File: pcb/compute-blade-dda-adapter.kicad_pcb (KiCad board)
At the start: 2 copper layers, 28 x 16.8 mm, 2 parts, among them J1 COMPUTE BLADE, J2 DDA GPS/RTC RIGHT-ANGLE

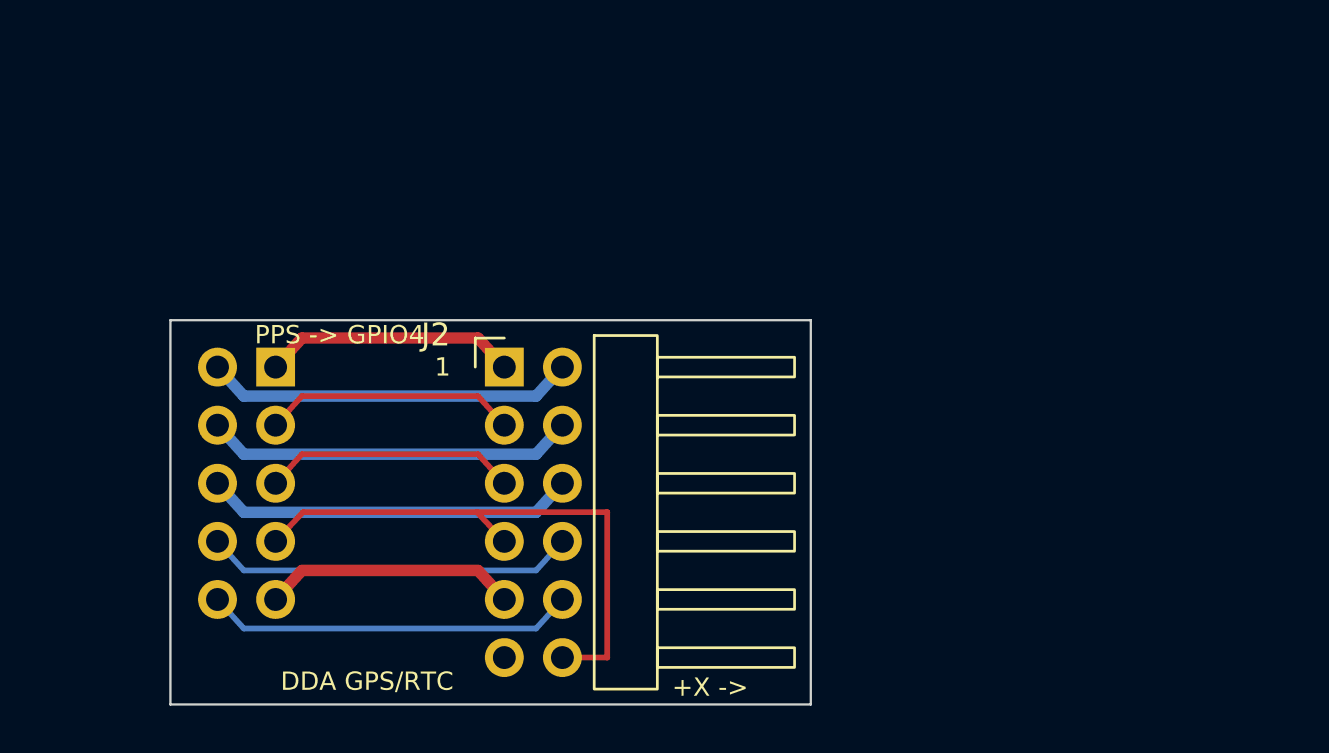
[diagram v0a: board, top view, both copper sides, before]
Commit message: Correct DDA rotation toward SSD side
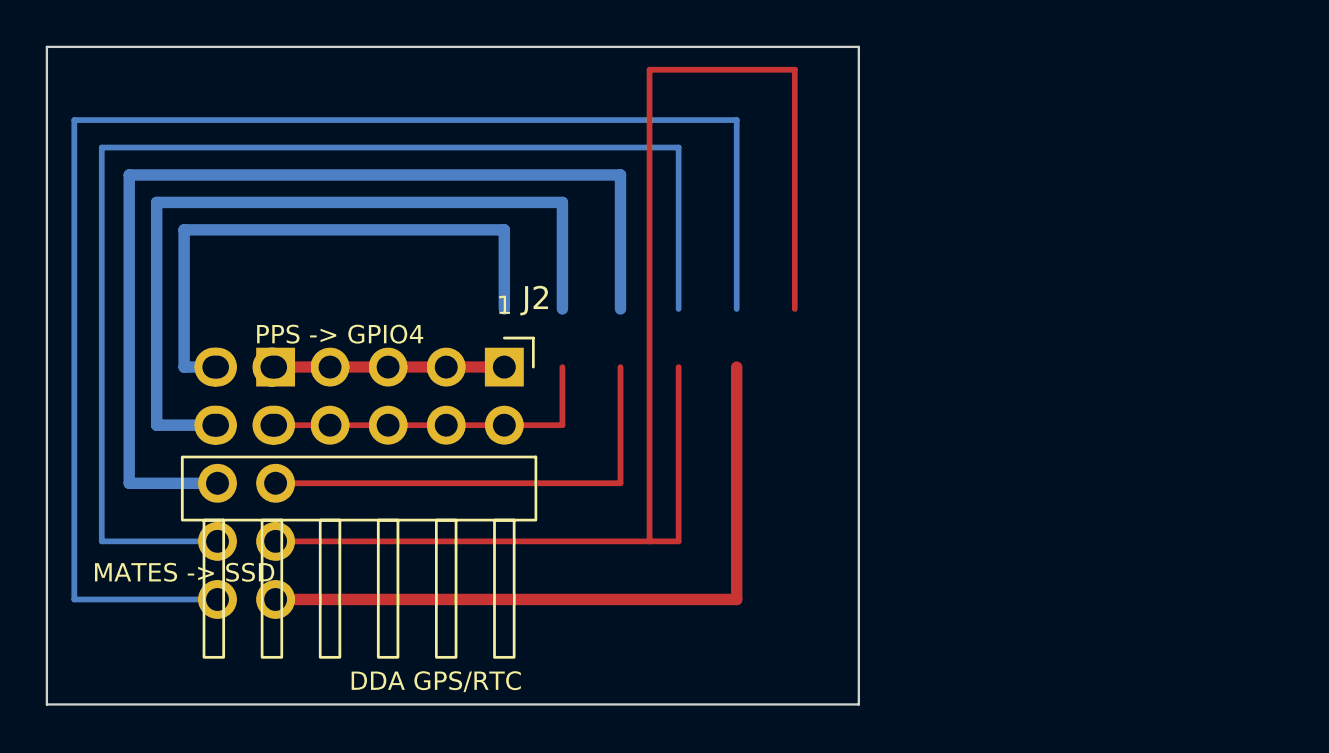
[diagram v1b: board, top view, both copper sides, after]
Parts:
- turned J2 to -90 degrees
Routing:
- net UART_RX_FROM_GPS_TX: track 16.2 -> 64.4 mm
- net UART_TX_TO_GPS_RX: track 16.2 -> 54.6 mm
- net PPS_GPIO4: track 25.1 -> 62.7 mm
- net GND_PIN6: track 16.2 -> 44.7 mm
- net GND_PIN9: track 11.1 -> 30.3 mm
- net 5V_PIN4: track 16.2 -> 34.8 mm
- net SCL_GPIO3: track 11.1 -> 20.2 mm
- net 5V_PIN2: track 16.2 -> 24.9 mm
- net SDA_GPIO2: track 11.1 -> 15.1 mm
- net 3V3: track 11.1 -> 10.0 mm
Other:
- board size 28 x 16.8 mm -> 35.5 x 28.8 mm
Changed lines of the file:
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@@
   (footprint "Connector_PinHeader_2.54mm:PinHeader_2x06_P2.54mm_Horizontal"
     (layer "F.Cu")
-    (at 110 60.16 0)
+    (at 110 60.16 -90)
     (descr "KiCad 10 standard 2x06 2.54 mm horizontal through-hole pin header, 6 mm mating pins")
     (tags "Through hole angled pin header THT 2x06 2.54mm double row")
@@
     (fp_text user "1" (at -2.7 0 0) (layer "F.SilkS")
  (effects (font (size 0.8 0.8) (thickness 0.14))))
-    (fp_text user "+X ->" (at 9 14 0) (layer "F.SilkS")
+    (fp_text user "MATES -> SSD" (at 9 14 0) (layer "F.SilkS")
  (effects (font (size 0.8 0.8) (thickness 0.13))))
     (pad "1" thru_hole rect (at 0 0)
@@
     (model "${KICAD10_3DMODEL_DIR}/Connector_PinHeader_2.54mm.3dshapes/PinHeader_2x06_P2.54mm_Horizontal.step" (offset (xyz 0 0 0)) (scale (xyz 1 1 1)) (rotate (xyz 0 0 0)))
   )
-  (gr_rect (start 95.4 58.11) (end 123.4 74.91)
+  (gr_rect (start 90 46.16) (end 125.5 74.91)
     (stroke (width 0.1) (type default)) (fill none) (layer "Edge.Cuts"))
-  (gr_text "DDA GPS/RTC" (at 104 73.9 0) (layer "F.SilkS")
+  (gr_text "DDA GPS/RTC" (at 107 73.9 0) (layer "F.SilkS")
     (effects (font (size 0.8 0.8) (thickness 0.13))))
   (gr_text "PPS -> GPIO4" (at 102.8 58.75 0) (layer "F.SilkS")
@@
   (gr_text "COMPUTE BLADE" (at 102.2 73.9 0) (layer "B.SilkS")
     (effects (font (size 0.8 0.8) (thickness 0.13)) (justify mirror)))
-  (segment (start 100 60.16) (end 101.15 58.89) (width 0.5) (layer "F.Cu") (net 1))
-  (segment (start 101.15 58.89) (end 108.85 58.89) (width 0.5) (layer "F.Cu") (net 1))
-  (segment (start 108.85 58.89) (end 110 60.16) (width 0.5) (layer "F.Cu") (net 1))
-  (segment (start 97.46 60.16) (end 98.61 61.43) (width 0.5) (layer "B.Cu") (net 2))
-  (segment (start 98.61 61.43) (end 111.39 61.43) (width 0.5) (layer "B.Cu") (net 2))
-  (segment (start 111.39 61.43) (end 112.54 60.16) (width 0.5) (layer "B.Cu") (net 2))
-  (segment (start 100 62.7) (end 101.15 61.43) (width 0.25) (layer "F.Cu") (net 3))
-  (segment (start 101.15 61.43) (end 108.85 61.43) (width 0.25) (layer "F.Cu") (net 3))
-  (segment (start 108.85 61.43) (end 110 62.7) (width 0.25) (layer "F.Cu") (net 3))
-  (segment (start 97.46 62.7) (end 98.61 63.97) (width 0.5) (layer "B.Cu") (net 4))
-  (segment (start 98.61 63.97) (end 111.39 63.97) (width 0.5) (layer "B.Cu") (net 4))
-  (segment (start 111.39 63.97) (end 112.54 62.7) (width 0.5) (layer "B.Cu") (net 4))
-  (segment (start 100 65.24) (end 101.15 63.97) (width 0.25) (layer "F.Cu") (net 5))
-  (segment (start 101.15 63.97) (end 108.85 63.97) (width 0.25) (layer "F.Cu") (net 5))
-  (segment (start 108.85 63.97) (end 110 65.24) (width 0.25) (layer "F.Cu") (net 5))
-  (segment (start 97.46 65.24) (end 98.61 66.51) (width 0.5) (layer "B.Cu") (net 6))
-  (segment (start 98.61 66.51) (end 111.39 66.51) (width 0.5) (layer "B.Cu") (net 6))
-  (segment (start 111.39 66.51) (end 112.54 65.24) (width 0.5) (layer "B.Cu") (net 6))
-  (segment (start 100 67.78) (end 101.2 66.5) (width 0.25) (layer "F.Cu") (net 7))
-  (segment (start 101.2 66.5) (end 108.8 66.5) (width 0.25) (layer "F.Cu") (net 7))
-  (segment (start 108.8 66.5) (end 110 67.78) (width 0.25) (layer "F.Cu") (net 7))
-  (segment (start 97.46 67.78) (end 98.61 69.05) (width 0.25) (layer "B.Cu") (net 8))
-  (segment (start 98.61 69.05) (end 111.39 69.05) (width 0.25) (layer "B.Cu") (net 8))
-  (segment (start 111.39 69.05) (end 112.54 67.78) (width 0.25) (layer "B.Cu") (net 8))
-  (segment (start 100 70.32) (end 101.15 69.05) (width 0.5) (layer "F.Cu") (net 9))
-  (segment (start 101.15 69.05) (end 108.85 69.05) (width 0.5) (layer "F.Cu") (net 9))
-  (segment (start 108.85 69.05) (end 110 70.32) (width 0.5) (layer "F.Cu") (net 9))
-  (segment (start 97.46 70.32) (end 98.61 71.59) (width 0.25) (layer "B.Cu") (net 10))
-  (segment (start 98.61 71.59) (end 111.39 71.59) (width 0.25) (layer "B.Cu") (net 10))
-  (segment (start 111.39 71.59) (end 112.54 70.32) (width 0.25) (layer "B.Cu") (net 10))
-  (segment (start 112.54 72.86) (end 114.5 72.86) (width 0.25) (layer "F.Cu") (net 7))
-  (segment (start 114.5 72.86) (end 114.5 66.5) (width 0.25) (layer "F.Cu") (net 7))
-  (segment (start 114.5 66.5) (end 108.8 66.5) (width 0.25) (layer "F.Cu") (net 7))
+  (segment (start 100 60.16) (end 110 60.16) (width 0.5) (layer "F.Cu") (net 1))
+  (segment (start 97.46 60.16) (end 96 60.16) (width 0.5) (layer "B.Cu") (net 2))
+  (segment (start 96 60.16) (end 96 54.16) (width 0.5) (layer "B.Cu") (net 2))
+  (segment (start 96 54.16) (end 110 54.16) (width 0.5) (layer "B.Cu") (net 2))
+  (segment (start 110 54.16) (end 110 57.62) (width 0.5) (layer "B.Cu") (net 2))
+  (segment (start 100 62.7) (end 112.54 62.7) (width 0.25) (layer "F.Cu") (net 3))
+  (segment (start 112.54 62.7) (end 112.54 60.16) (width 0.25) (layer "F.Cu") (net 3))
+  (segment (start 97.46 62.7) (end 94.8 62.7) (width 0.5) (layer "B.Cu") (net 4))
+  (segment (start 94.8 62.7) (end 94.8 52.96) (width 0.5) (layer "B.Cu") (net 4))
+  (segment (start 94.8 52.96) (end 112.54 52.96) (width 0.5) (layer "B.Cu") (net 4))
+  (segment (start 112.54 52.96) (end 112.54 57.62) (width 0.5) (layer "B.Cu") (net 4))
+  (segment (start 100 65.24) (end 115.08 65.24) (width 0.25) (layer "F.Cu") (net 5))
+  (segment (start 115.08 65.24) (end 115.08 60.16) (width 0.25) (layer "F.Cu") (net 5))
+  (segment (start 97.46 65.24) (end 93.6 65.24) (width 0.5) (layer "B.Cu") (net 6))
+  (segment (start 93.6 65.24) (end 93.6 51.76) (width 0.5) (layer "B.Cu") (net 6))
+  (segment (start 93.6 51.76) (end 115.08 51.76) (width 0.5) (layer "B.Cu") (net 6))
+  (segment (start 115.08 51.76) (end 115.08 57.62) (width 0.5) (layer "B.Cu") (net 6))
+  (segment (start 100 67.78) (end 116.35 67.78) (width 0.25) (layer "F.Cu") (net 7))
+  (segment (start 116.35 67.78) (end 117.62 67.78) (width 0.25) (layer "F.Cu") (net 7))
+  (segment (start 117.62 67.78) (end 117.62 60.16) (width 0.25) (layer "F.Cu") (net 7))
+  (segment (start 97.46 67.78) (end 92.4 67.78) (width 0.25) (layer "B.Cu") (net 8))
+  (segment (start 92.4 67.78) (end 92.4 50.56) (width 0.25) (layer "B.Cu") (net 8))
+  (segment (start 92.4 50.56) (end 117.62 50.56) (width 0.25) (layer "B.Cu") (net 8))
+  (segment (start 117.62 50.56) (end 117.62 57.62) (width 0.25) (layer "B.Cu") (net 8))
+  (segment (start 100 70.32) (end 120.16 70.32) (width 0.5) (layer "F.Cu") (net 9))
+  (segment (start 120.16 70.32) (end 120.16 60.16) (width 0.5) (layer "F.Cu") (net 9))
+  (segment (start 97.46 70.32) (end 91.2 70.32) (width 0.25) (layer "B.Cu") (net 10))
+  (segment (start 91.2 70.32) (end 91.2 49.36) (width 0.25) (layer "B.Cu") (net 10))
+  (segment (start 91.2 49.36) (end 120.16 49.36) (width 0.25) (layer "B.Cu") (net 10))
+  (segment (start 120.16 49.36) (end 120.16 57.62) (width 0.25) (layer "B.Cu") (net 10))
+  (segment (start 122.7 57.62) (end 122.7 47.16) (width 0.25) (layer "F.Cu") (net 7))
+  (segment (start 122.7 47.16) (end 116.35 47.16) (width 0.25) (layer "F.Cu") (net 7))
+  (segment (start 116.35 47.16) (end 116.35 67.78) (width 0.25) (layer "F.Cu") (net 7))
 )

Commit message: Use KiCad-correct J2 rotation convention
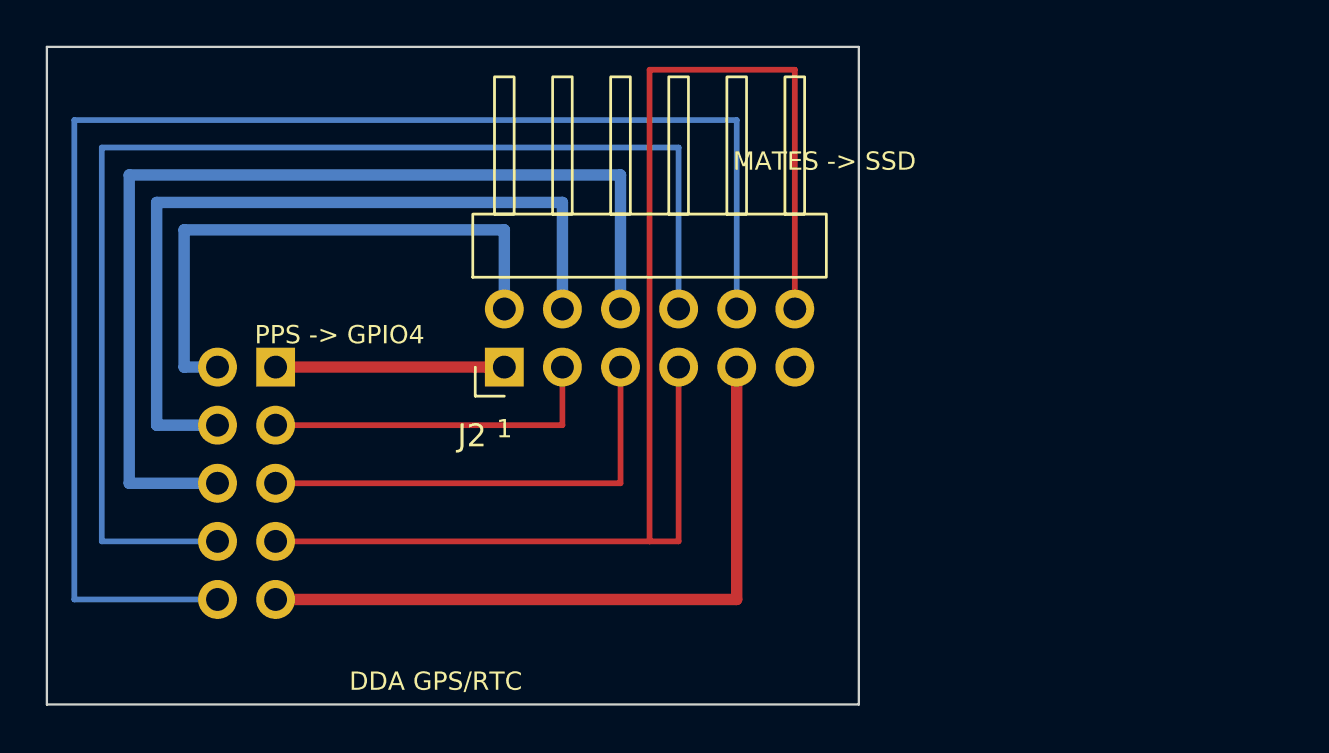
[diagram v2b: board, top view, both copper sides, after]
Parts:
- turned J2 to 90 degrees
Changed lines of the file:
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@@
   (footprint "Connector_PinHeader_2.54mm:PinHeader_2x06_P2.54mm_Horizontal"
     (layer "F.Cu")
-    (at 110 60.16 -90)
+    (at 110 60.16 90)
     (descr "KiCad 10 standard 2x06 2.54 mm horizontal through-hole pin header, 6 mm mating pins")
     (tags "Through hole angled pin header THT 2x06 2.54mm double row")

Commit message: Move upright DDA assembly to positive Y
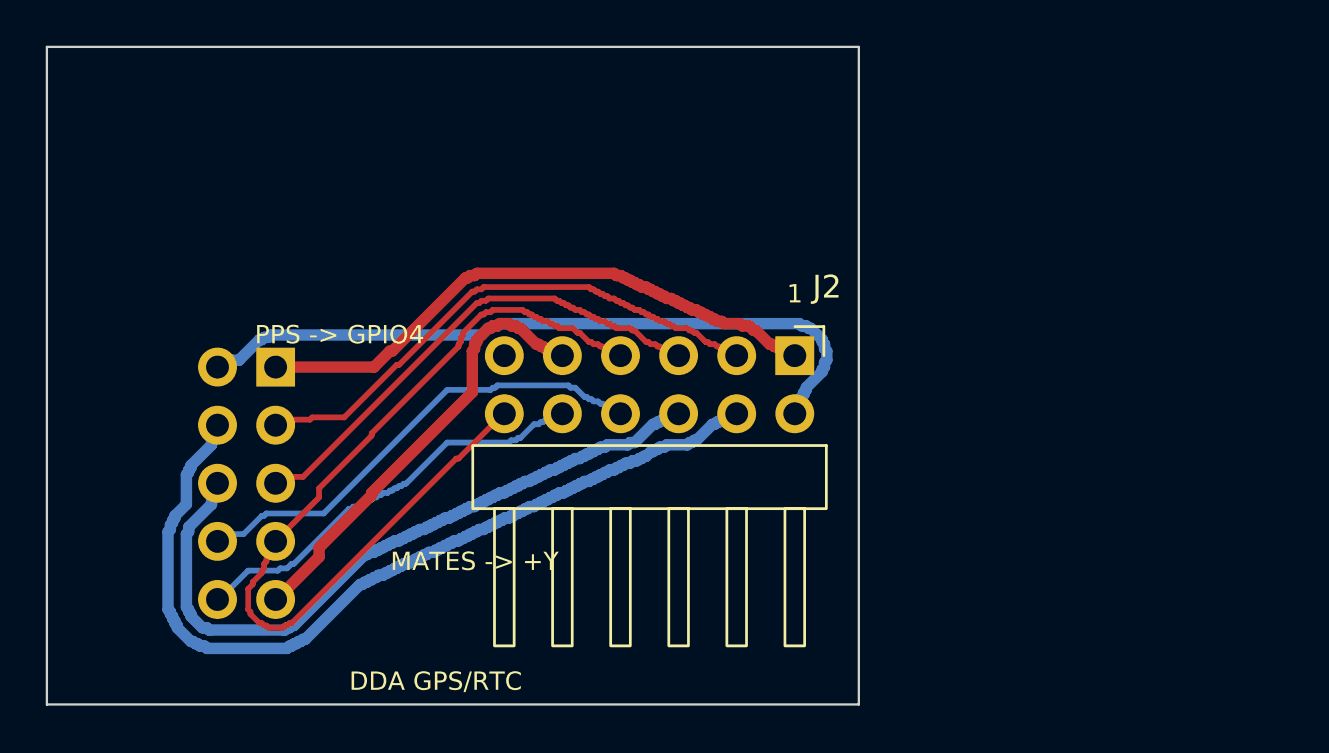
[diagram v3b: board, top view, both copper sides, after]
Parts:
- moved J2 12.7 mm to (122.7, 59.7), turned to -90 degrees
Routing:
- net UART_RX_FROM_GPS_TX: track 64.4 -> 18.5 mm
- net UART_TX_TO_GPS_RX: track 54.6 -> 21.0 mm
- net PPS_GPIO4: track 62.7 -> 39.7 mm
- net 3V3: track 10.0 -> 25.9 mm
- net GND_PIN6: track 44.7 -> 32.0 mm
- net GND_PIN9: track 30.3 -> 19.7 mm
- net SDA_GPIO2: track 15.1 -> 24.0 mm
- net 5V_PIN2: track 24.9 -> 31.4 mm
- net 5V_PIN4: track 34.8 -> 39.1 mm
- net SCL_GPIO3: track 20.2 -> 22.0 mm

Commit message: Add clearance-safe connector escape routing
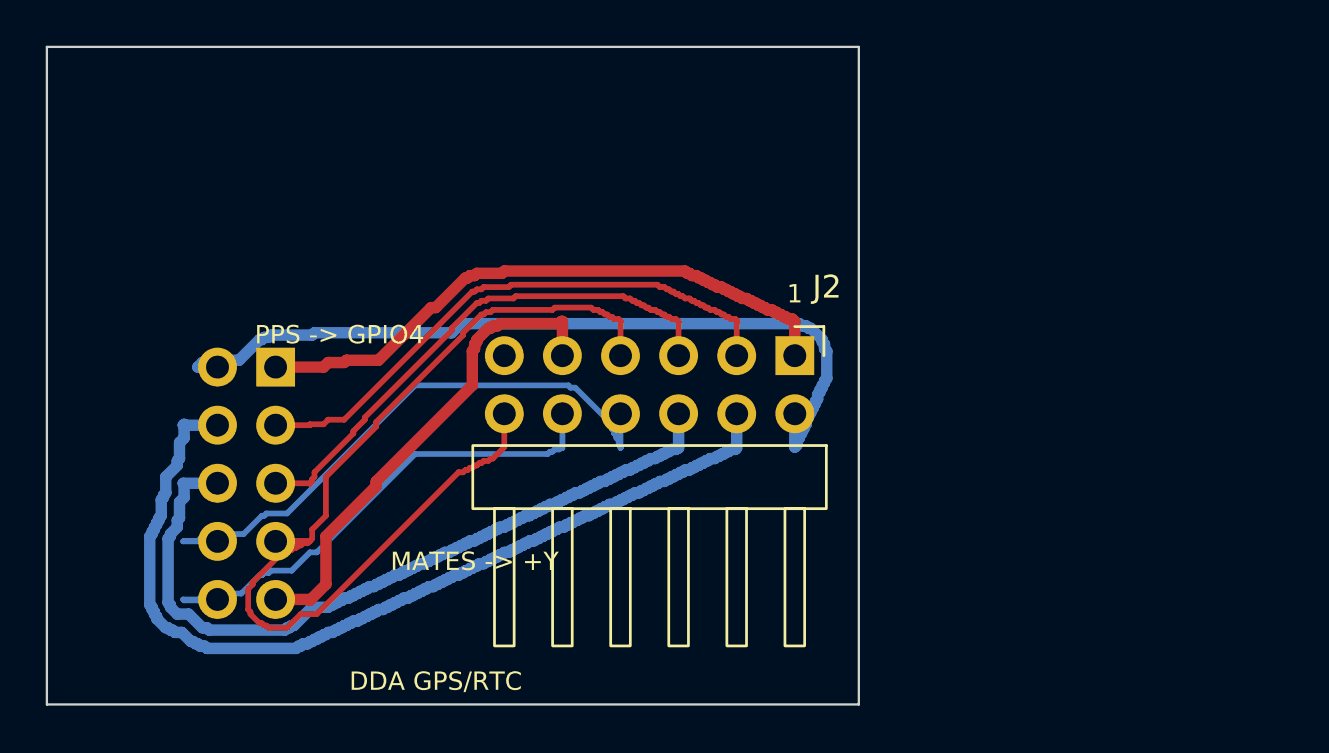
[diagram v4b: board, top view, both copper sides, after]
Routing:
- net UART_TX_TO_GPS_RX: track 21.0 -> 26.5 mm
- net PPS_GPIO4: track 39.7 -> 44.9 mm
- net 5V_PIN2: track 31.4 -> 36.1 mm
- net UART_RX_FROM_GPS_TX: track 18.5 -> 22.4 mm
- net GND_PIN6: track 32.0 -> 34.7 mm
- net 5V_PIN4: track 39.1 -> 41.8 mm
- net GND_PIN9: track 19.7 -> 21.5 mm
- net SCL_GPIO3: track 22.0 -> 23.3 mm
- net 3V3: track 25.9 -> 26.9 mm
- net SDA_GPIO2: track 24.0 -> 25.0 mm
